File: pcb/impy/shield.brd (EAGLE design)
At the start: 133 x 107 mm, 117 parts, among them J1 USB-2410-06, J2 SI-60062-F, J3 5V, U1 AD5933YRS, U10 LTC3406AB, U11 23LCV1024-I/SN, U12 MIC2009A-1YM6, U13 ADG725BSU, U14 ADG725BSU, U2 ADG704BRM, U3 AD8656ARZ, U4 M24C08WMN, U5 ADG706BRU, U6 DP83848I, U7 MIC2009A-1YM6, U8 AT25DF081A-SS, U9 SST25VF080B-80-4I-S2

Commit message: * pcb/impy: (shield.sch) Change value of main power switch current limit resistor (to 510R which sets a 400mA limit). This switch does not carry the USB power, so the limit need not be that high.
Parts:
- R12: value 300R -> 510R
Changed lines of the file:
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@@
 <attribute name="RS" value="485-8061" x="35.2425" y="17.4625" size="1.778" layer="27" rot="R270" display="off"/>
 </element>
-<element name="R12" library="rcl" package="R0603" value="300R" x="16.1925" y="43.815" rot="R180"/>
+<element name="R12" library="rcl" package="R0603" value="510R" x="16.1925" y="43.815" rot="R180"/>
 <element name="R13" library="rcl" package="R0603" value="510R" x="41.275" y="10.16"/>
 <element name="U10" library="parts" package="TSOT23-5" value="LTC3406AB" x="13.6525" y="53.975">

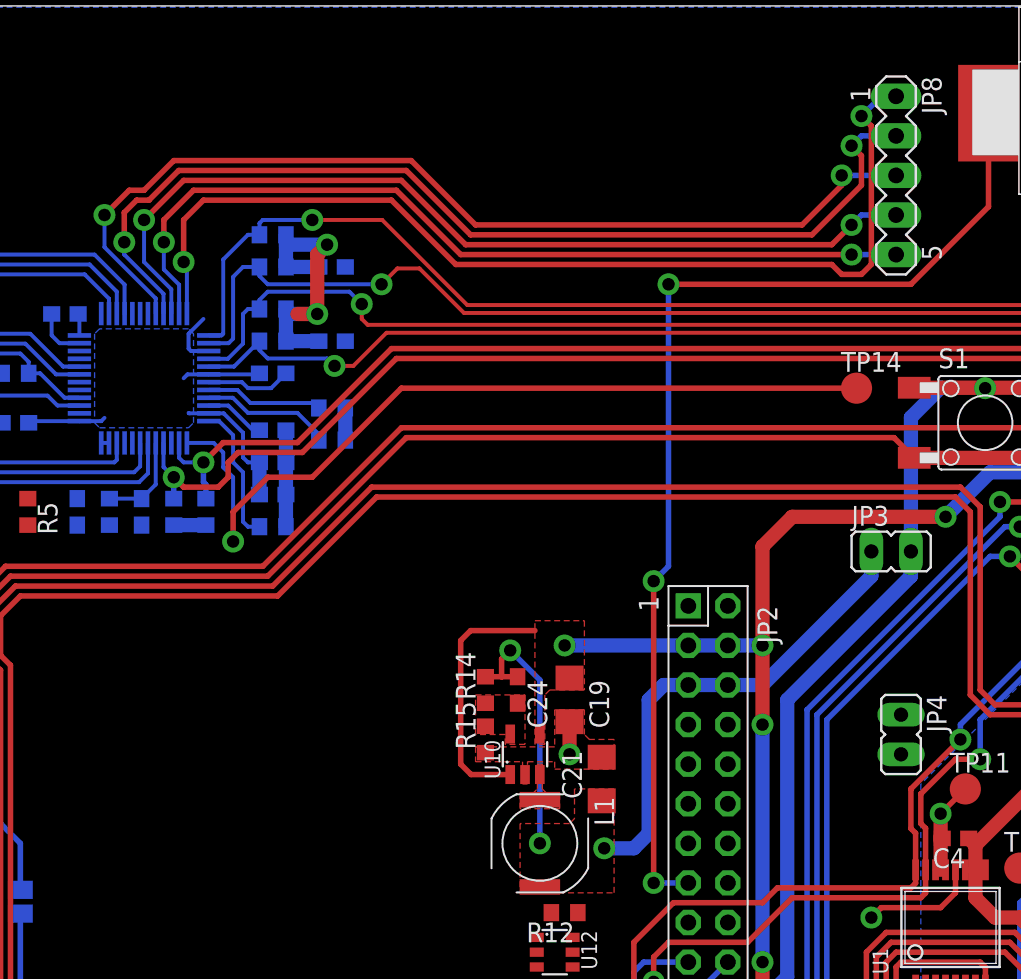
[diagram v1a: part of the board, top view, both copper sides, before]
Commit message: * pcb/impy: (shield.brd) Change layout of Ethernet PHY JTAG traces, move them all to bottom layer to avoid unnecessary vias.
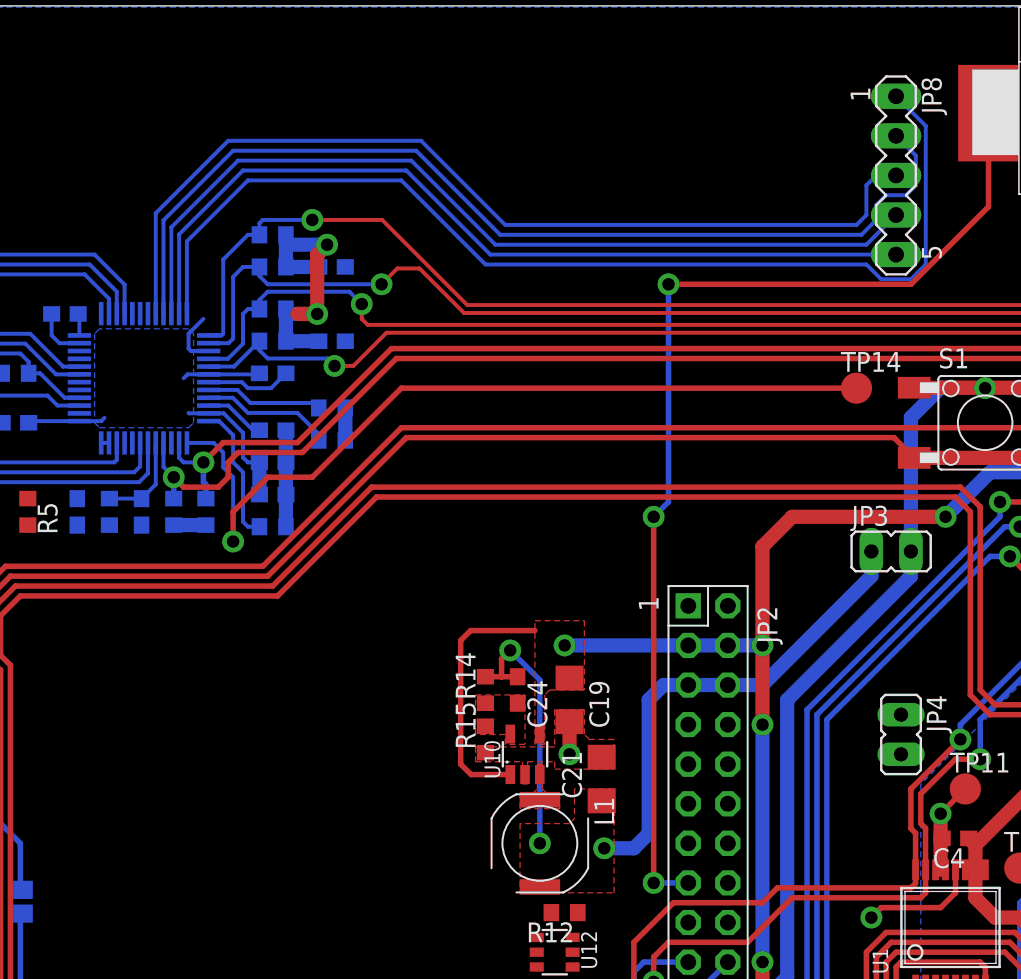
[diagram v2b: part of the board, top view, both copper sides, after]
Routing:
- net N$29: track 63.3 -> 60.5 mm, vias 2 -> 0
- net N$27: track 65.5 -> 68.3 mm, vias 2 -> 0
- net N$30: track 58.5 -> 56.8 mm, vias 2 -> 0
- net N$28: track 64.9 -> 63.9 mm, vias 2 -> 0
- net N$31: track 55.9 -> 55.0 mm, vias 2 -> 0

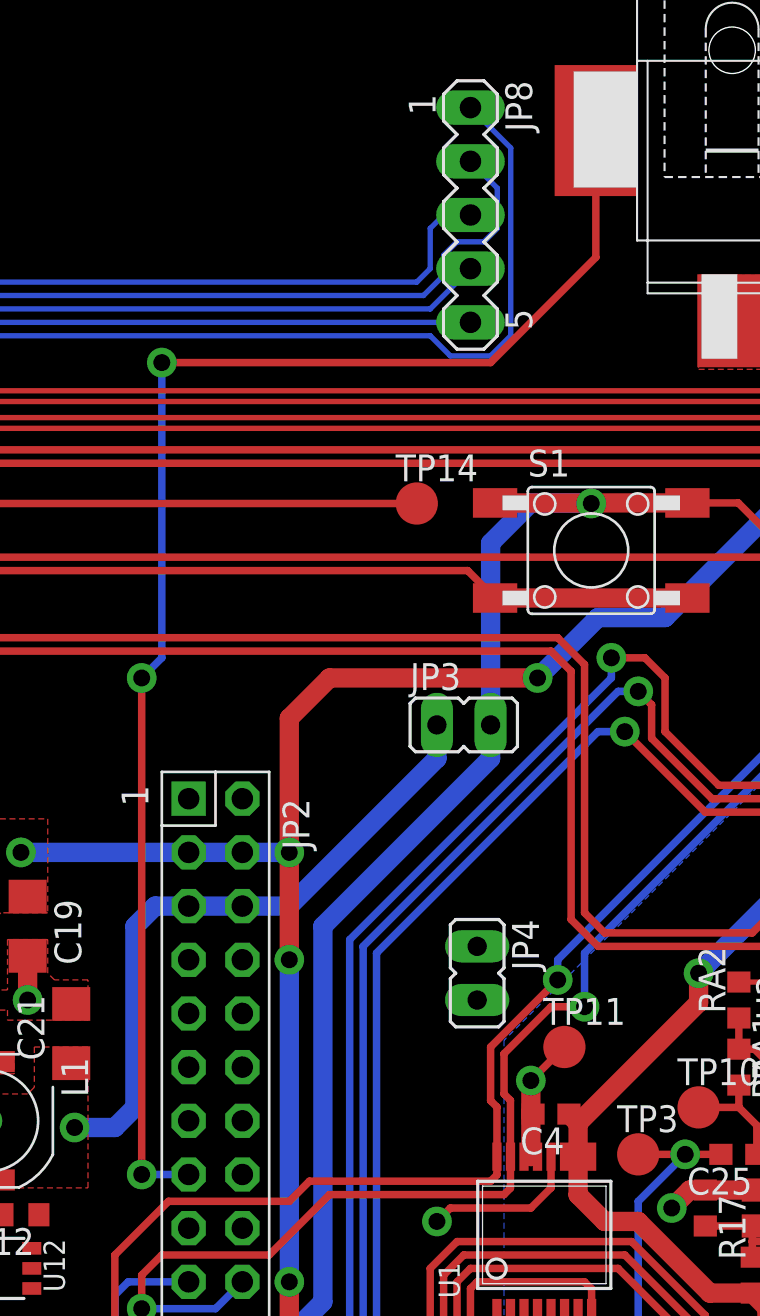
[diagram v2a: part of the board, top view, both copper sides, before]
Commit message: * pcb/impy: (shield.brd) Improve layout of power jack detect signal.
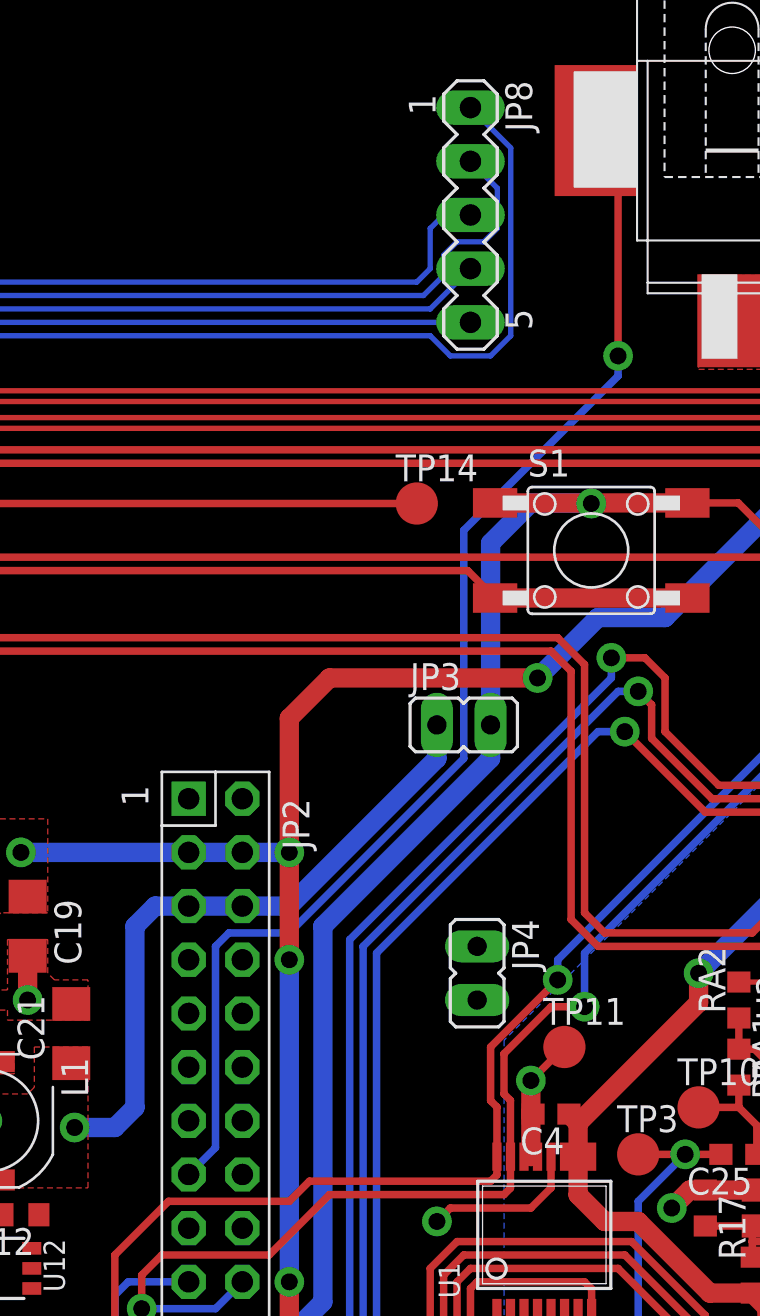
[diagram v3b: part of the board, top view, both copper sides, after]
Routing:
- net PE2: track 69.6 -> 59.9 mm, vias 3 -> 1
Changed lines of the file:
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@@
 <contactref element="JP2" pad="15"/>
 <contactref element="J3" pad="3"/>
-<wire x1="43.3975" y1="95.1175" x2="43.3975" y2="89.1175" width="0.3556" layer="1"/>
-<wire x1="43.3975" y1="89.1175" x2="38.4175" y2="84.1375" width="0.3556" layer="1"/>
-<wire x1="38.4175" y1="84.1375" x2="22.86" y2="84.1375" width="0.3556" layer="1"/>
-<via x="22.86" y="84.1375" extent="1-16" drill="0.8" shape="octagon"/>
-<wire x1="24.13" y1="45.72" x2="21.9075" y2="45.72" width="0.3556" layer="16"/>
-<via x="21.9075" y="45.72" extent="1-16" drill="0.8" shape="octagon"/>
-<wire x1="21.9075" y1="45.72" x2="21.9075" y2="69.215" width="0.3556" layer="1"/>
-<via x="21.9075" y="69.215" extent="1-16" drill="0.8" shape="octagon"/>
-<wire x1="21.9075" y1="69.215" x2="22.86" y2="70.1675" width="0.3556" layer="16"/>
-<wire x1="22.86" y1="70.1675" x2="22.86" y2="84.1375" width="0.3556" layer="16"/>
+<wire x1="24.13" y1="45.72" x2="25.4" y2="46.99" width="0.3556" layer="16"/>
+<wire x1="25.4" y1="46.99" x2="25.4" y2="56.515" width="0.3556" layer="16"/>
+<wire x1="25.4" y1="56.515" x2="26.035" y2="57.15" width="0.3556" layer="16"/>
+<wire x1="26.035" y1="57.15" x2="28.8925" y2="57.15" width="0.3556" layer="16"/>
+<wire x1="28.8925" y1="57.15" x2="37.1475" y2="65.405" width="0.3556" layer="16"/>
+<wire x1="37.1475" y1="65.405" x2="37.1475" y2="76.2" width="0.3556" layer="16"/>
+<wire x1="37.1475" y1="76.2" x2="44.45" y2="83.5025" width="0.3556" layer="16"/>
+<wire x1="44.45" y1="83.5025" x2="44.45" y2="84.455" width="0.3556" layer="16"/>
+<via x="44.45" y="84.455" extent="1-16" drill="0.8" shape="octagon"/>
+<wire x1="44.45" y1="84.455" x2="44.45" y2="94.065" width="0.3556" layer="1"/>
+<wire x1="44.45" y1="94.065" x2="43.3975" y2="95.1175" width="0.3556" layer="1"/>
 </signal>
 <signal name="PB10">

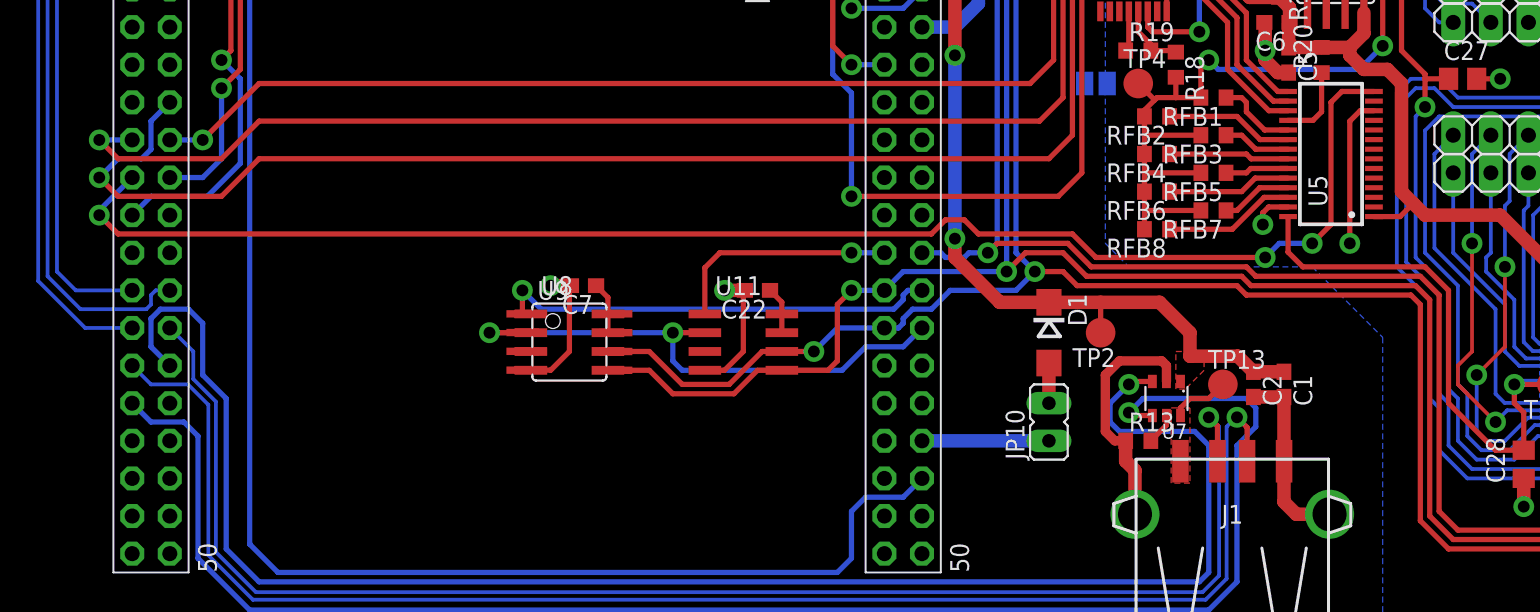
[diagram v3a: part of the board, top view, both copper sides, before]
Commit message: * pcb/impy: (shield.sch) Remove unnecessary feedback resistor selection signal (PE11).   (shield.brd) Remove PE11 trace and straighten some other ones.
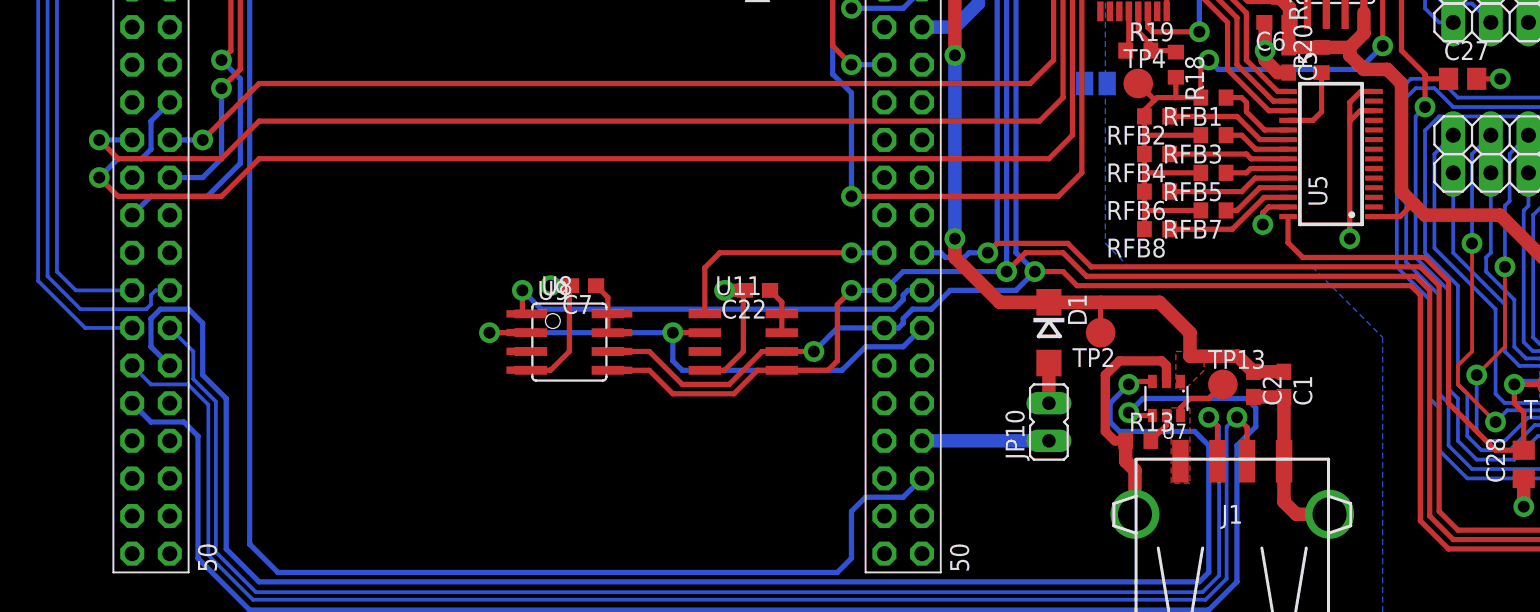
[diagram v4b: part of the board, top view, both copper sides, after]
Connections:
- net AGND: now also U5.14
- net PE11: no longer U5.14
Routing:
- net PE11: track 101.0 -> 0.00 mm, vias 3 -> 0
- net AGND: track 52.2 -> 55.1 mm
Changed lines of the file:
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@@
 <wire x1="70.8025" y1="2.8575" x2="62.23" y2="2.8575" width="0.3556" layer="1"/>
 <wire x1="62.23" y1="2.8575" x2="60.325" y2="4.7625" width="0.3556" layer="1"/>
-<wire x1="60.325" y1="4.7625" x2="60.325" y2="19.3675" width="0.3556" layer="1"/>
-<wire x1="60.325" y1="19.3675" x2="59.69" y2="20.0025" width="0.3556" layer="1"/>
-<wire x1="59.69" y1="20.0025" x2="48.5775" y2="20.0025" width="0.3556" layer="1"/>
-<wire x1="48.5775" y1="20.0025" x2="47.9425" y2="20.6375" width="0.3556" layer="1"/>
-<wire x1="47.9425" y1="20.6375" x2="37.1475" y2="20.6375" width="0.3556" layer="1"/>
+<wire x1="60.325" y1="4.7625" x2="60.325" y2="20.0025" width="0.3556" layer="1"/>
+<wire x1="60.325" y1="20.0025" x2="59.69" y2="20.6375" width="0.3556" layer="1"/>
+<wire x1="59.69" y1="20.6375" x2="37.1475" y2="20.6375" width="0.3556" layer="1"/>
 <wire x1="37.1475" y1="20.6375" x2="36.195" y2="21.59" width="0.3556" layer="1"/>
 <wire x1="36.195" y1="21.59" x2="34.29" y2="21.59" width="0.3556" layer="1"/>
@@
 <wire x1="70.485" y1="3.4925" x2="62.5475" y2="3.4925" width="0.3556" layer="1"/>
 <wire x1="62.5475" y1="3.4925" x2="60.96" y2="5.08" width="0.3556" layer="1"/>
-<wire x1="60.96" y1="5.08" x2="60.96" y2="19.685" width="0.3556" layer="1"/>
-<wire x1="60.96" y1="19.685" x2="60.0075" y2="20.6375" width="0.3556" layer="1"/>
-<wire x1="60.0075" y1="20.6375" x2="48.895" y2="20.6375" width="0.3556" layer="1"/>
-<wire x1="48.895" y1="20.6375" x2="48.26" y2="21.2725" width="0.3556" layer="1"/>
-<wire x1="48.26" y1="21.2725" x2="37.7825" y2="21.2725" width="0.3556" layer="1"/>
+<wire x1="60.96" y1="5.08" x2="60.96" y2="20.32" width="0.3556" layer="1"/>
+<wire x1="60.96" y1="20.32" x2="60.0075" y2="21.2725" width="0.3556" layer="1"/>
+<wire x1="60.0075" y1="21.2725" x2="37.7825" y2="21.2725" width="0.3556" layer="1"/>
 <wire x1="37.7825" y1="21.2725" x2="36.195" y2="22.86" width="0.3556" layer="1"/>
 <wire x1="36.195" y1="22.86" x2="33.655" y2="22.86" width="0.3556" layer="1"/>
@@
 <signal name="PE11">
 <contactref element="JP1" pad="29"/>
-<contactref element="U5" pad="14"/>
-<via x="53.0225" y="23.495" extent="1-16" drill="0.8" shape="octagon"/>
-<wire x1="53.0225" y1="23.495" x2="50.8" y2="23.495" width="0.3556" layer="16"/>
-<wire x1="50.8" y1="23.495" x2="49.8475" y2="22.5425" width="0.3556" layer="16"/>
-<via x="49.8475" y="22.5425" extent="1-16" drill="0.8" shape="octagon"/>
-<wire x1="49.8475" y1="22.5425" x2="38.4175" y2="22.5425" width="0.3556" layer="1"/>
-<wire x1="38.4175" y1="22.5425" x2="36.83" y2="24.13" width="0.3556" layer="1"/>
-<wire x1="27.305" y1="24.13" x2="-27.6225" y2="24.13" width="0.3556" layer="1"/>
-<wire x1="-27.6225" y1="24.13" x2="-28.8925" y2="25.4" width="0.3556" layer="1"/>
-<via x="-28.8925" y="25.4" extent="1-16" drill="0.8" shape="octagon"/>
-<wire x1="-28.8925" y1="25.4" x2="-28.8925" y2="25.7175" width="0.3556" layer="16"/>
-<wire x1="-28.8925" y1="25.7175" x2="-26.67" y2="27.94" width="0.3556" layer="16"/>
-<wire x1="57.1925" y1="33.7525" x2="55.025" y2="33.7525" width="0.3556" layer="1"/>
-<wire x1="55.025" y1="33.7525" x2="54.2925" y2="33.02" width="0.3556" layer="1"/>
-<wire x1="54.2925" y1="33.02" x2="54.2925" y2="24.765" width="0.3556" layer="1"/>
-<wire x1="54.2925" y1="24.765" x2="53.0225" y2="23.495" width="0.3556" layer="1"/>
-<wire x1="27.305" y1="24.13" x2="28.2575" y2="25.0825" width="0.3556" layer="1"/>
-<wire x1="28.2575" y1="25.0825" x2="29.5275" y2="25.0825" width="0.3556" layer="1"/>
-<wire x1="29.5275" y1="25.0825" x2="30.48" y2="24.13" width="0.3556" layer="1"/>
-<wire x1="30.48" y1="24.13" x2="36.83" y2="24.13" width="0.3556" layer="1"/>
 </signal>
 <signal name="PE12">
@@
 <wire x1="49.79125" y1="38.4175" x2="49.8475" y2="38.36125" width="0.9144" layer="1"/>
 <wire x1="49.8475" y1="38.36125" x2="49.8475" y2="36.5125" width="0.9144" layer="1"/>
+<wire x1="55.5625" y1="33.02" x2="55.5625" y2="31.75" width="0.3556" layer="1"/>
+<via x="55.5625" y="23.8125" extent="1-16" drill="0.8" shape="octagon"/>
+<wire x1="55.5625" y1="31.75" x2="55.5625" y2="23.8125" width="0.3556" layer="1"/>
+<wire x1="64.1325" y1="34.6075" x2="65.7225" y2="34.6075" width="0.3556" layer="1"/>
+<via x="65.7225" y="34.6075" extent="1-16" drill="0.8" shape="octagon"/>
+<contactref element="U5" pad="14"/>
+<wire x1="57.1925" y1="33.7525" x2="56.295" y2="33.7525" width="0.3556" layer="1"/>
+<wire x1="56.295" y1="33.7525" x2="55.5625" y2="33.02" width="0.3556" layer="1"/>
 <wire x1="57.1925" y1="32.4525" x2="56.265" y2="32.4525" width="0.3556" layer="1"/>
 <wire x1="56.265" y1="32.4525" x2="55.5625" y2="31.75" width="0.3556" layer="1"/>
-<wire x1="55.5625" y1="31.75" x2="55.5625" y2="23.495" width="0.3556" layer="1"/>
-<via x="55.5625" y="23.495" extent="1-16" drill="0.8" shape="octagon"/>
-<wire x1="64.1325" y1="34.6075" x2="65.7225" y2="34.6075" width="0.3556" layer="1"/>
-<via x="65.7225" y="34.6075" extent="1-16" drill="0.8" shape="octagon"/>
 </signal>
 <signal name="PA2">
@@
 <wire x1="70.1675" y1="4.1275" x2="62.865" y2="4.1275" width="0.3556" layer="1"/>
 <wire x1="62.865" y1="4.1275" x2="61.595" y2="5.3975" width="0.3556" layer="1"/>
-<wire x1="61.595" y1="5.3975" x2="61.595" y2="20.0025" width="0.3556" layer="1"/>
-<wire x1="61.595" y1="20.0025" x2="60.325" y2="21.2725" width="0.3556" layer="1"/>
-<wire x1="60.325" y1="21.2725" x2="49.2125" y2="21.2725" width="0.3556" layer="1"/>
-<wire x1="49.2125" y1="21.2725" x2="48.5775" y2="21.9075" width="0.3556" layer="1"/>
-<wire x1="48.5775" y1="21.9075" x2="38.1" y2="21.9075" width="0.3556" layer="1"/>
+<wire x1="61.595" y1="5.3975" x2="61.595" y2="20.6375" width="0.3556" layer="1"/>
+<wire x1="61.595" y1="20.6375" x2="60.325" y2="21.9075" width="0.3556" layer="1"/>
+<wire x1="60.325" y1="21.9075" x2="38.1" y2="21.9075" width="0.3556" layer="1"/>
 <wire x1="38.1" y1="21.9075" x2="36.5125" y2="23.495" width="0.3556" layer="1"/>
 <wire x1="36.5125" y1="23.495" x2="31.75" y2="23.495" width="0.3556" layer="1"/>
@@
 <wire x1="66.675" y1="12.7" x2="67.31" y2="12.065" width="0.3556" layer="1"/>
 <wire x1="67.31" y1="12.065" x2="67.31" y2="9.5225" width="0.3556" layer="1"/>
-<wire x1="51.3925" y1="25.3025" x2="51.3925" y2="22.9025" width="0.3556" layer="1"/>
-<wire x1="51.3925" y1="22.9025" x2="52.3875" y2="21.9075" width="0.3556" layer="1"/>
-<wire x1="52.3875" y1="21.9075" x2="60.6425" y2="21.9075" width="0.3556" layer="1"/>
-<wire x1="60.6425" y1="21.9075" x2="62.23" y2="20.32" width="0.3556" layer="1"/>
-<wire x1="62.23" y1="20.32" x2="62.23" y2="12.7" width="0.3556" layer="1"/>
+<wire x1="51.3925" y1="25.3025" x2="51.3925" y2="23.5375" width="0.3556" layer="1"/>
+<wire x1="51.3925" y1="23.5375" x2="52.3875" y2="22.5425" width="0.3556" layer="1"/>
+<wire x1="52.3875" y1="22.5425" x2="60.6425" y2="22.5425" width="0.3556" layer="1"/>
+<wire x1="60.6425" y1="22.5425" x2="62.23" y2="20.955" width="0.3556" layer="1"/>
+<wire x1="62.23" y1="20.955" x2="62.23" y2="12.7" width="0.3556" layer="1"/>
 <wire x1="62.23" y1="12.7" x2="65.405" y2="9.525" width="0.3556" layer="1"/>
 <wire x1="65.405" y1="9.525" x2="67.3075" y2="9.525" width="0.3556" layer="1"/>
